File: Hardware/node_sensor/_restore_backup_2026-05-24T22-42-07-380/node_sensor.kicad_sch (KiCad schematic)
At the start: 14 parts, among them J1 Conn_Jack-DC, J2 Pump, J3 Light, U1 DevKitESP32, U2 DHT11, U3 BH1750, U4 ADS1115, U5 DS3231, U6 Soil-Moisture, U7 Soil-Moisture, U8 Soil-Moisture, U9 Soil-Moisture

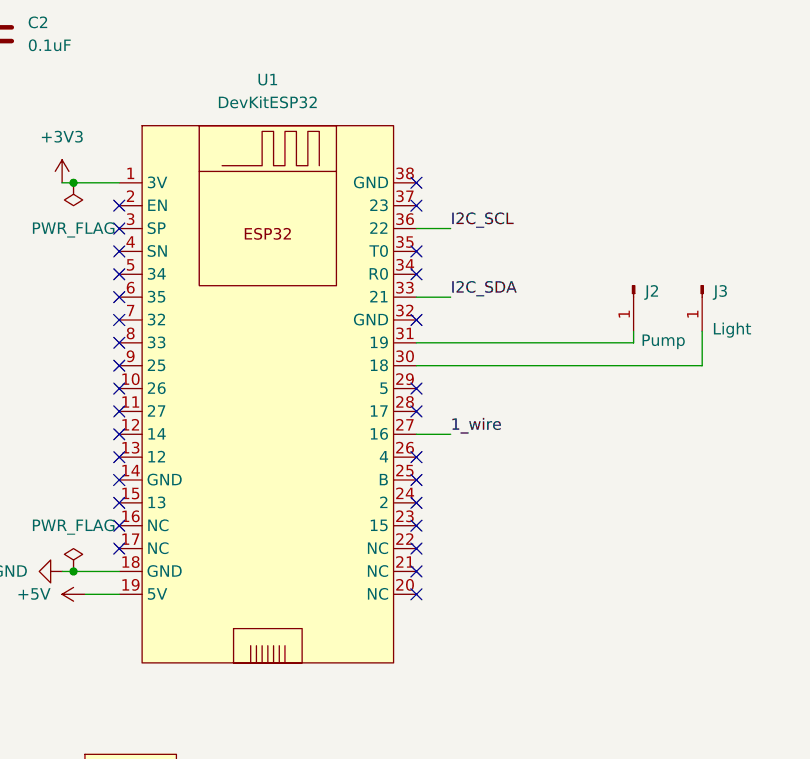
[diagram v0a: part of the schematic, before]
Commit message: updated hardware + fixed conflict Gatway
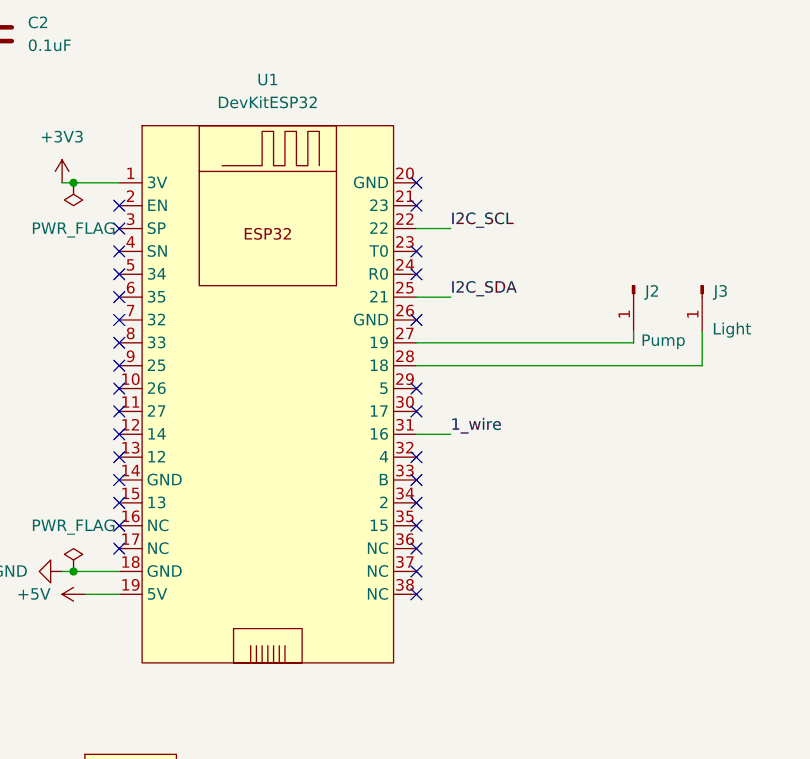
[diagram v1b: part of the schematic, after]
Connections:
- net 1_wire: now also U1.31 (16); no longer U1.27 (16)
- net I2C_SCL: now also U1.22; no longer U1.36 (22)
- net I2C_SDA: now also U1.25 (21); no longer U1.33 (21)
- net at U1.28 (18): now also J3.1 (Pin_1)
- net at U1.30 (17): no longer J3.1 (Pin_1)
- net at J2.1 (Pin_1): now also U1.27 (19); no longer U1.31 (19)
